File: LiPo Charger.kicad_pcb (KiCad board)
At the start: 2 copper layers, 20 x 19 mm, 21 parts, among them J1 Battery_conn_in, J2 Battery_conn_out, J3 Charger_conn, U1 BQ24090DGQ, U2 XB8089D

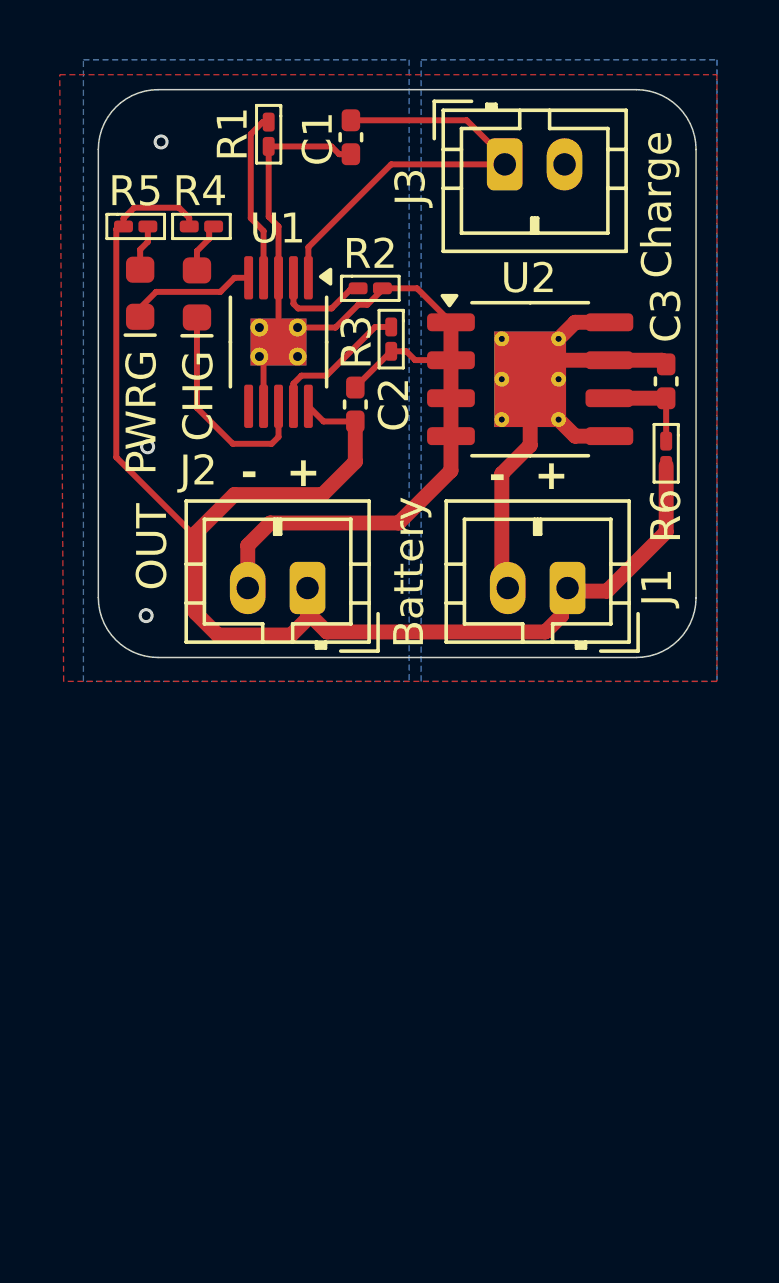
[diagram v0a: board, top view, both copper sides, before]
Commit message: feat: battery active balancing is now added.
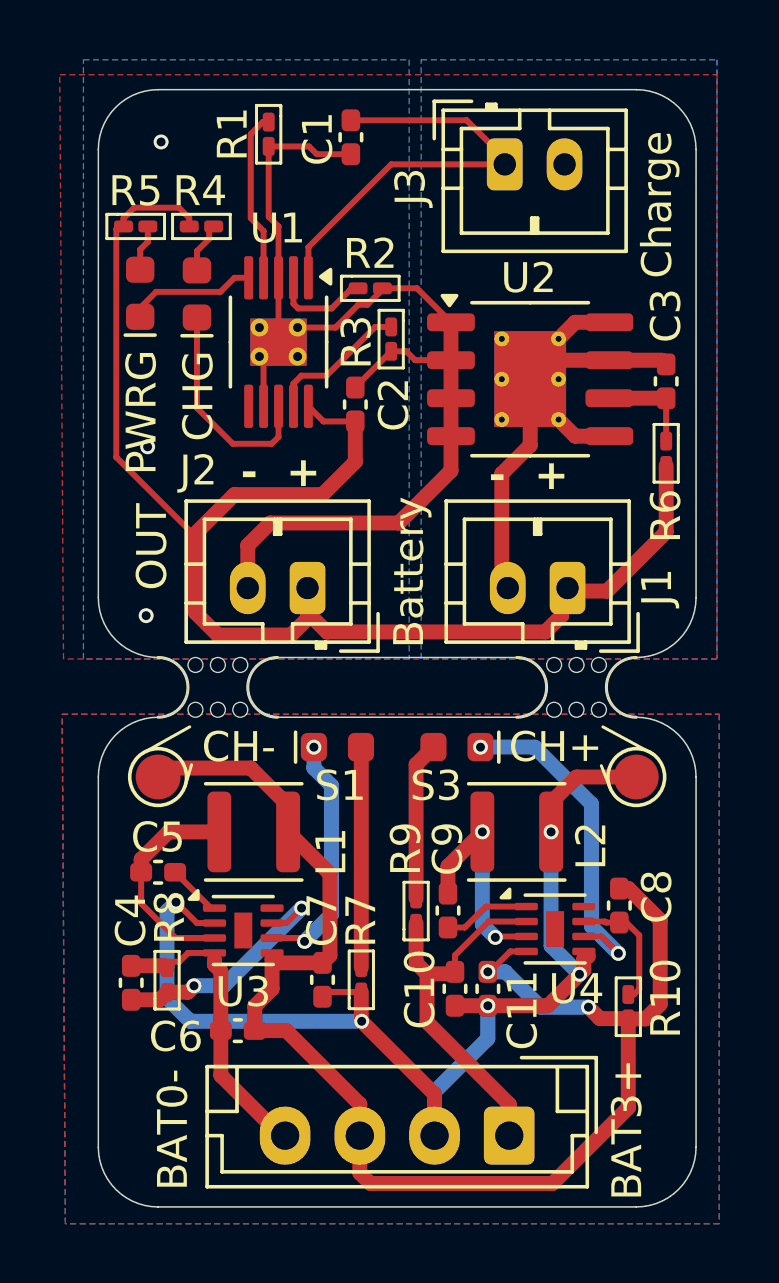
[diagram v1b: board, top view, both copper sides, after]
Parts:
- added C10: 10uF, Capacitor_SMD:C_0402_1005Metric_Pad0.74x0.62mm_HandSolder, F.Cu at (82.4, 71.6)
- added C11: 10uF, Capacitor_SMD:C_0402_1005Metric_Pad0.74x0.62mm_HandSolder, F.Cu at (83.5, 71.6)
- added C4: 1nF, Capacitor_SMD:C_0402_1005Metric_Pad0.74x0.62mm_HandSolder, F.Cu at (71.6, 71.4)
- added C5: 10nF, Capacitor_SMD:C_0402_1005Metric_Pad0.74x0.62mm_HandSolder, F.Cu at (72.5, 67.7)
- added C6: 10uF, Capacitor_SMD:C_0402_1005Metric_Pad0.74x0.62mm_HandSolder, F.Cu at (75.2, 73.0)
- added C7: 10uF, Capacitor_SMD:C_0402_1005Metric_Pad0.74x0.62mm_HandSolder, F.Cu at (78.0, 71.3)
- added C8: 1nF, Capacitor_SMD:C_0402_1005Metric_Pad0.74x0.62mm_HandSolder, F.Cu at (87.9, 68.8)
- added C9: 10nF, Capacitor_SMD:C_0402_1005Metric_Pad0.74x0.62mm_HandSolder, F.Cu at (82.2, 69.0)
- added D3: Red, SparkFun-LED:LED_0603_1608Metric_Red, F.Cu at (78.5, 63.5)
- added D4: Red, SparkFun-LED:LED_0603_1608Metric_Red, F.Cu at (82.5, 63.5)
- added G***: LOGO, LOGO, B.Cu at (87.8, 66.5)
- added J4: Conn_01x04_batteries, Connector_JST:JST_EH_B4B-EH-A_1x04_P2.50mm_Vertical, F.Cu at (84.2, 76.5)
- added L1: 1uH, Inductor_SMD:L_Sunlord_SWPA3010S, F.Cu at (75.7, 66.3)
- added L2: 1uH, Inductor_SMD:L_Sunlord_SWPA3010S, F.Cu at (84.5, 66.3)
- added R10: 51K, PCM_Resistor_SMD_AKL:R_0201_0603Metric_Pad0.64x0.40mm_HandSolder, F.Cu at (88.2, 72.2)
- added R7: 1k5, PCM_Resistor_SMD_AKL:R_0201_0603Metric_Pad0.64x0.40mm_HandSolder, F.Cu at (79.3, 71.3)
- added R8: 51K, PCM_Resistor_SMD_AKL:R_0201_0603Metric_Pad0.64x0.40mm_HandSolder, F.Cu at (72.8, 71.3)
- added R9: 1k5, PCM_Resistor_SMD_AKL:R_0201_0603Metric_Pad0.64x0.40mm_HandSolder, F.Cu at (81.1, 69.0)
- added REF**: WEEE-Logo_4.2x6mm_SilkScreen, Symbol:WEEE-Logo_4.2x6mm_SilkScreen, B.Cu at (87.4, 74.1)
- added TP1: TestPoint, TestPoint:TestPoint_Pad_D1.5mm, F.Cu at (88.5, 64.5)
- added TP2: TestPoint, TestPoint:TestPoint_Pad_D1.5mm, F.Cu at (72.5, 64.5)
- added U3: ~, Package_DFN_QFN:DFN-8-1EP_2x2mm_P0.5mm_EP0.6x1.2mm, F.Cu at (75.3, 69.6)
- added U4: ~, Package_DFN_QFN:DFN-8-1EP_2x2mm_P0.5mm_EP0.6x1.2mm, F.Cu at (85.8, 69.6)
- added mouse-bite-2mm-slot: VAL**, MouseBites:mouse-bite-2mm-slot, F.Cu at (86.5, 61.5)
- added mouse-bite-2mm-slot: VAL**, MouseBites:mouse-bite-2mm-slot, F.Cu at (74.5, 61.5)
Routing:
- net Net-(J4-Pin_3): track 0.00 -> 48.6 mm, vias 0 -> 2
- net Net-(J4-Pin_2): track 0.00 -> 38.8 mm, vias 0 -> 5
- net Net-(J4-Pin_1): track 0.00 -> 12.8 mm
- net Net-(D4-K): track 0.00 -> 11.3 mm, vias 0 -> 2
- net Net-(J4-Pin_4): track 0.00 -> 10.4 mm
- net Net-(D3-K): track 0.00 -> 8.25 mm, vias 0 -> 2
- net Net-(U3-ISET): track 0.00 -> 8.17 mm, vias 0 -> 2
- net Net-(U3-SW): track 0.00 -> 7.41 mm
- net Net-(D3-A): track 0.00 -> 7.38 mm
- net Net-(U4-SW): track 0.00 -> 7.30 mm, vias 0 -> 2
- net Net-(D4-A): track 0.00 -> 5.32 mm
- net Net-(U4-ISET): track 0.00 -> 4.29 mm
- net Net-(U4-BATC): track 0.00 -> 2.91 mm
- net Net-(U3-BATC): track 0.00 -> 1.82 mm
- added copper zone on B.Cu, net (none)
- added copper zone on F.Cu, net (none)
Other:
- board size 20 x 19 mm -> 20 x 37.4 mm
- board text added: "3S Battery Balancer v1.0"
- board text added: "BAT0-"
- board text added: "BAT3+"
- board text added: "BATTERY0-"
- board text added: "BATTERY1+"
- board text added: "BATTERY2+"
- board text added: "BATTERY3+"
- board text added: "CH+"
- board text added: "CH-"
- board text added: "S1"
- board text added: "S3"

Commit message: making production files for PCBA.
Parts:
- U3, U4: value ~ -> ETA3000
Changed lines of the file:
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@@
 			)
 		)
-		(property "Value" "~"
+		(property "Value" "ETA3000"
 			(at 0 1.95 0)
 			(layer "F.Fab")
@@
 			)
 		)
-		(property "Value" "~"
+		(property "Value" "ETA3000"
 			(at 0 1.95 0)
 			(layer "F.Fab")
